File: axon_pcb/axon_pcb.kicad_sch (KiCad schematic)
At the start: 108 parts, among them J1 USB_C_Receptacle, J2 AVR_ISP Header, K1 KEYSW, K10 KEYSW, K11 KEYSW, K12 KEYSW, K13 KEYSW, K14 KEYSW, K15 KEYSW, K16 KEYSW, K17 KEYSW, K18 KEYSW, K19 KEYSW, K2 KEYSW, K20 KEYSW, K21 KEYSW, K22 KEYSW, K23 KEYSW, K24 KEYSW, K25 KEYSW, K26 KEYSW, K27 KEYSW, K28 KEYSW, K29 KEYSW, K3 KEYSW, K30 KEYSW, K31 KEYSW, K32 KEYSW, K33 KEYSW, K34 KEYSW, K35 KEYSW, K36 KEYSW, K37 KEYSW, K38 KEYSW, K39 KEYSW, K4 KEYSW, K40 KEYSW, K41 KEYSW, K42 KEYSW, K43 KEYSW, K44 KEYSW, K45 KEYSW, K46 KEYSW, K5 KEYSW, K6 KEYSW, K7 KEYSW, K8 KEYSW, K9 KEYSW, SW1 RESET, SW2 BOOT, U1 ATmega328P-PU, X1 16MHz

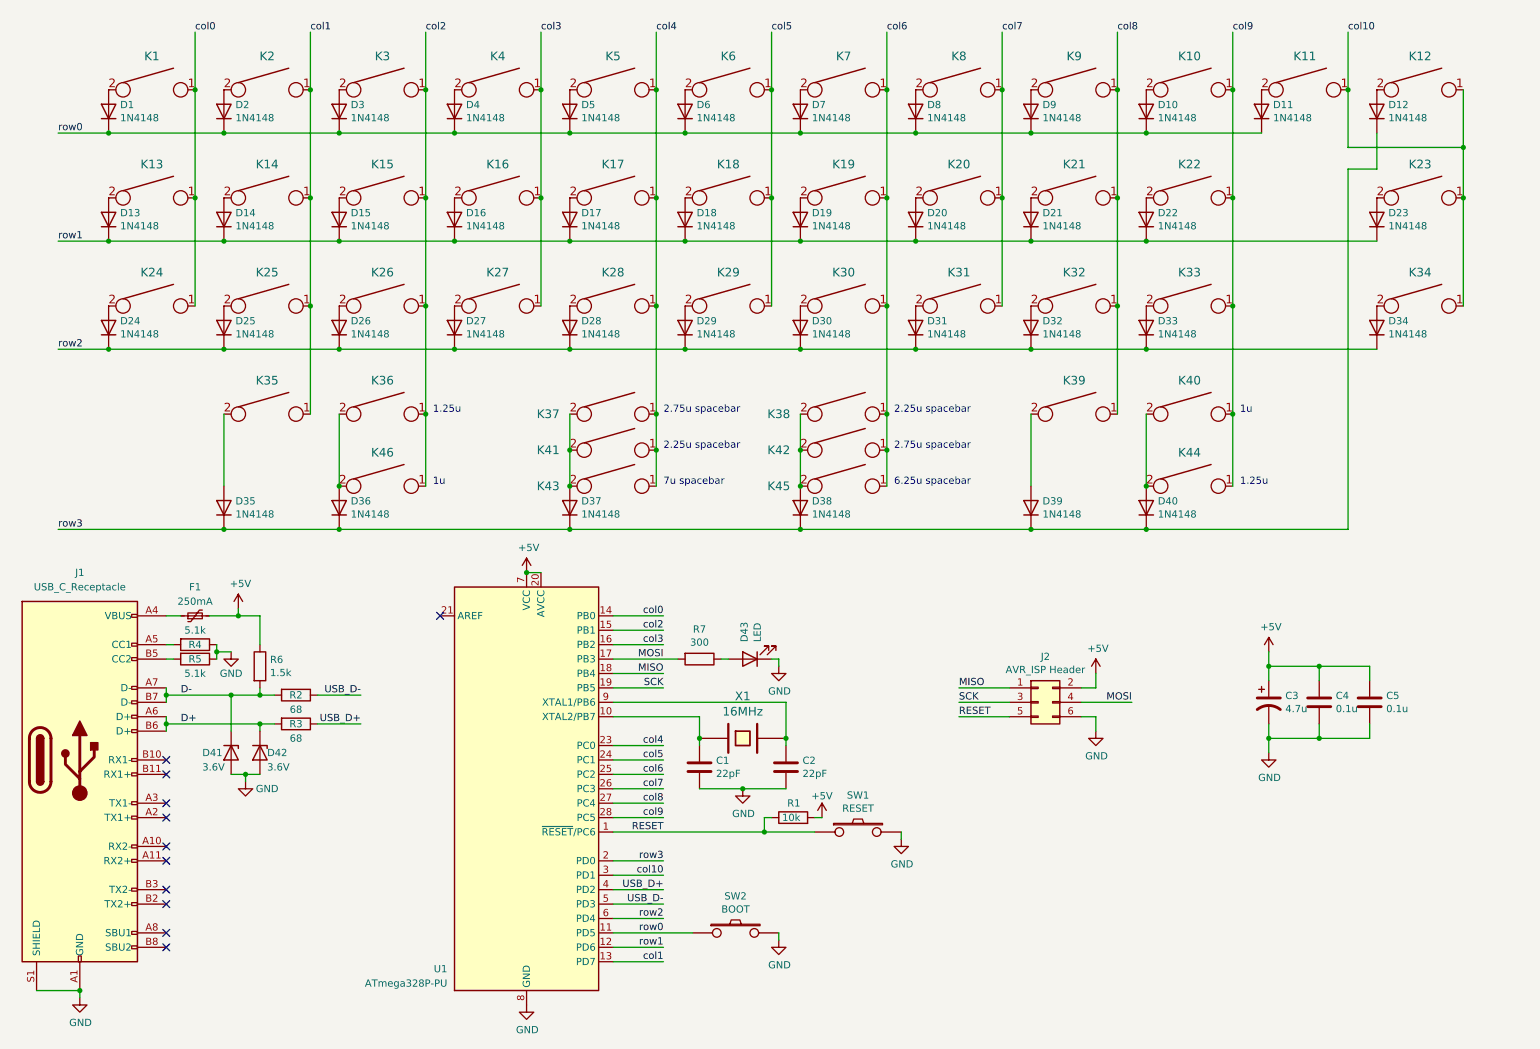
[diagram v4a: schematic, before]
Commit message: enable hardware pwm led dimming
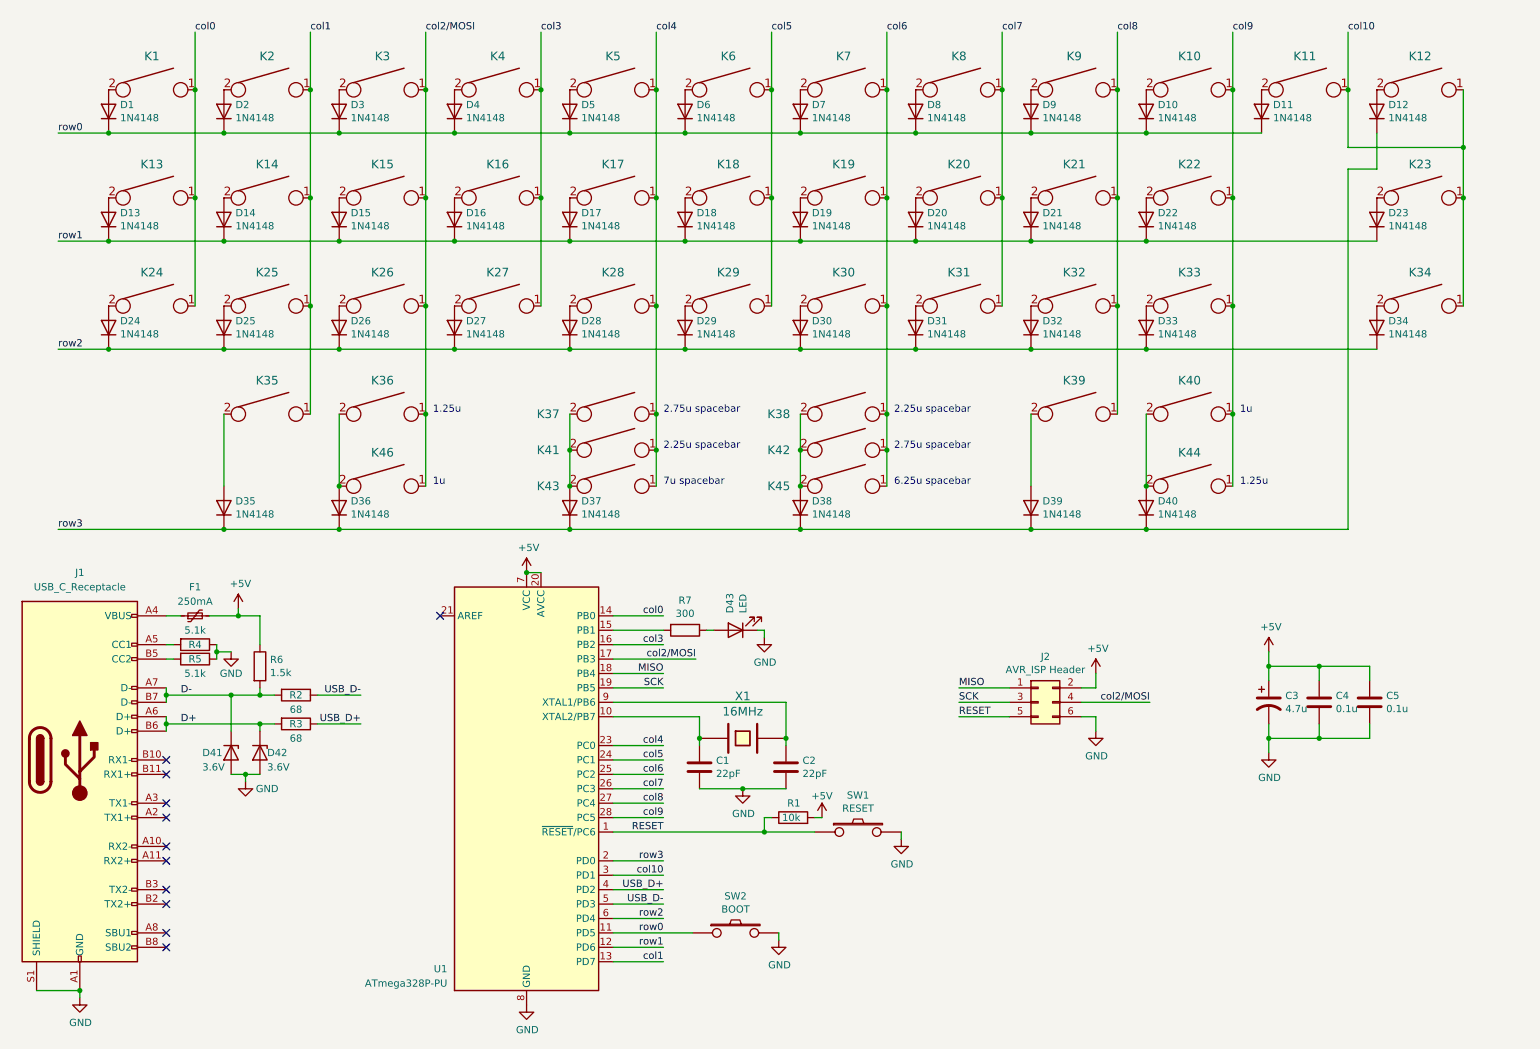
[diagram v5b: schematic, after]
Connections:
- net MOSI renamed col2/MOSI
- net col2/MOSI: now also K15.1, K26.1, K3.1, K36.1, K46.1; no longer R7.2
- removed net col2: K15.1, K26.1, K3.1, K36.1, K46.1, U1.15 (PB1)
- new net: R7.2, U1.15 (PB1)
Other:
- moved on the sheet: D43, R7
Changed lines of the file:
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@@
     (stroke (width 0) (type default) (color 0 0 0 0))
   )
-  (wire (pts (xy 140.97 130.81) (xy 142.24 130.81))
+  (wire (pts (xy 138.43 125.73) (xy 139.7 125.73))
     (stroke (width 0) (type default) (color 0 0 0 0))
   )
@@
     (stroke (width 0) (type default) (color 0 0 0 0))
   )
-  (wire (pts (xy 149.86 130.81) (xy 151.13 130.81))
+  (wire (pts (xy 147.32 125.73) (xy 148.59 125.73))
     (stroke (width 0) (type default) (color 0 0 0 0))
   )
@@
     (stroke (width 0) (type default) (color 0 0 0 0))
   )
-  (wire (pts (xy 121.92 130.81) (xy 133.35 130.81))
+  (wire (pts (xy 121.92 130.81) (xy 136.525 130.81))
     (stroke (width 0) (type default) (color 0 0 0 0))
   )
@@
     (stroke (width 0) (type default) (color 0 0 0 0))
   )
-  (wire (pts (xy 204.47 138.43) (xy 213.36 138.43))
+  (wire (pts (xy 204.47 138.43) (xy 216.535 138.43))
     (stroke (width 0) (type default) (color 0 0 0 0))
   )
@@
     (stroke (width 0) (type default) (color 0 0 0 0))
   )
-  (wire (pts (xy 151.13 130.81) (xy 151.13 132.08))
+  (wire (pts (xy 148.59 125.73) (xy 148.59 127))
     (stroke (width 0) (type default) (color 0 0 0 0))
   )
@@
     (effects (font (size 1.27 1.27)) (justify right bottom))
   )
-  (label "col2" (at 130.81 125.73 180)
-    (effects (font (size 1.27 1.27)) (justify right bottom))
-  )
   (label "col4" (at 129.54 20.32 0)
     (effects (font (size 1.27 1.27)) (justify left bottom))
@@
     (effects (font (size 1.27 1.27)) (justify right bottom))
   )
-  (label "MOSI" (at 130.81 130.81 180)
+  (label "col2{slash}MOSI" (at 136.525 130.81 180)
     (effects (font (size 1.27 1.27)) (justify right bottom))
   )
@@
     (effects (font (size 1.27 1.27)) (justify left bottom))
   )
-  (label "col2" (at 88.9 20.32 0)
+  (label "col2{slash}MOSI" (at 88.9 20.32 0)
     (effects (font (size 1.27 1.27)) (justify left bottom))
   )
@@
     (effects (font (size 1.27 1.27)) (justify left bottom))
   )
-  (label "MOSI" (at 213.36 138.43 180)
+  (label "col2{slash}MOSI" (at 216.535 138.43 180)
     (effects (font (size 1.27 1.27)) (justify right bottom))
   )
@@
     (pin "1")
   )
-  (symbol (lib_id "Device:R") (at 137.16 130.81 270) (unit 1)
-    (in_bom yes) (on_board yes)
-    (property "Reference" "R7" (id 0) (at 137.16 125.5522 90))
-    (property "Value" "300" (id 1) (at 137.16 127.8636 90))
-    (property "Footprint" "Resistor_THT:R_Axial_DIN0204_L3.6mm_D1.6mm_P5.08mm_Horizontal" (id 2) (at 137.16 129.032 90)
-      (effects (font (size 1.27 1.27)) hide)
-    )
-    (property "Datasheet" "~" (id 3) (at 137.16 130.81 0)
-      (effects (font (size 1.27 1.27)) hide)
-    )
-    (pin "1")
-    (pin "2")
-  )
-  (symbol (lib_id "Device:LED") (at 146.05 130.81 180) (unit 1)
-    (in_bom yes) (on_board yes)
-    (property "Reference" "D43" (id 0) (at 145.0594 127.8128 90)
-      (effects (font (size 1.27 1.27)) (justify right))
-    )
-    (property "Value" "LED" (id 1) (at 147.3708 127.8128 90)
-      (effects (font (size 1.27 1.27)) (justify right))
-    )
-    (property "Footprint" "LED_THT:LED_D5.0mm" (id 2) (at 146.05 130.81 0)
-      (effects (font (size 1.27 1.27)) hide)
-    )
-    (property "Datasheet" "~" (id 3) (at 146.05 130.81 0)
-      (effects (font (size 1.27 1.27)) hide)
-    )
-    (pin "1")
-    (pin "2")
-  )
-  (symbol (lib_id "power:GND") (at 151.13 132.08 0) (unit 1)
-    (in_bom yes) (on_board yes)
-    (property "Reference" "#PWR0111" (id 0) (at 151.13 138.43 0)
-      (effects (font (size 1.27 1.27)) hide)
-    )
-    (property "Value" "GND" (id 1) (at 151.257 136.4742 0))
-    (property "Footprint" "" (id 2) (at 151.13 132.08 0)
-      (effects (font (size 1.27 1.27)) hide)
-    )
-    (property "Datasheet" "" (id 3) (at 151.13 132.08 0)
-      (effects (font (size 1.27 1.27)) hide)
-    )
+  (symbol (lib_id "Device:R") (at 134.62 125.73 270) (unit 1)
+    (in_bom yes) (on_board yes)
+    (property "Reference" "R7" (id 0) (at 134.62 120.4722 90))
+    (property "Value" "300" (id 1) (at 134.62 122.7836 90))
+    (property "Footprint" "Resistor_THT:R_Axial_DIN0204_L3.6mm_D1.6mm_P5.08mm_Horizontal" (id 2) (at 134.62 123.952 90)
+      (effects (font (size 1.27 1.27)) hide)
+    )
+    (property "Datasheet" "~" (id 3) (at 134.62 125.73 0)
+      (effects (font (size 1.27 1.27)) hide)
+    )
+    (pin "1")
+    (pin "2")
+  )
+  (symbol (lib_id "Device:LED") (at 143.51 125.73 180) (unit 1)
+    (in_bom yes) (on_board yes)
+    (property "Reference" "D43" (id 0) (at 142.5194 122.7328 90)
+      (effects (font (size 1.27 1.27)) (justify right))
+    )
+    (property "Value" "LED" (id 1) (at 144.8308 122.7328 90)
+      (effects (font (size 1.27 1.27)) (justify right))
+    )
+    (property "Footprint" "LED_THT:LED_D5.0mm" (id 2) (at 143.51 125.73 0)
+      (effects (font (size 1.27 1.27)) hide)
+    )
+    (property "Datasheet" "~" (id 3) (at 143.51 125.73 0)
+      (effects (font (size 1.27 1.27)) hide)
+    )
+    (pin "1")
+    (pin "2")
+  )
+  (symbol (lib_id "power:GND") (at 148.59 127 0) (unit 1)
+    (in_bom yes) (on_board yes)
+    (property "Reference" "#PWR0111" (id 0) (at 148.59 133.35 0)
+      (effects (font (size 1.27 1.27)) hide)
+    )
+    (property "Value" "GND" (id 1) (at 148.717 131.3942 0))
+    (property "Footprint" "" (id 2) (at 148.59 127 0)
+      (effects (font (size 1.27 1.27)) hide)
+    )
+    (property "Datasheet" "" (id 3) (at 148.59 127 0)
+      (effects (font (size 1.27 1.27)) hide)
+    )

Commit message: add encoder support
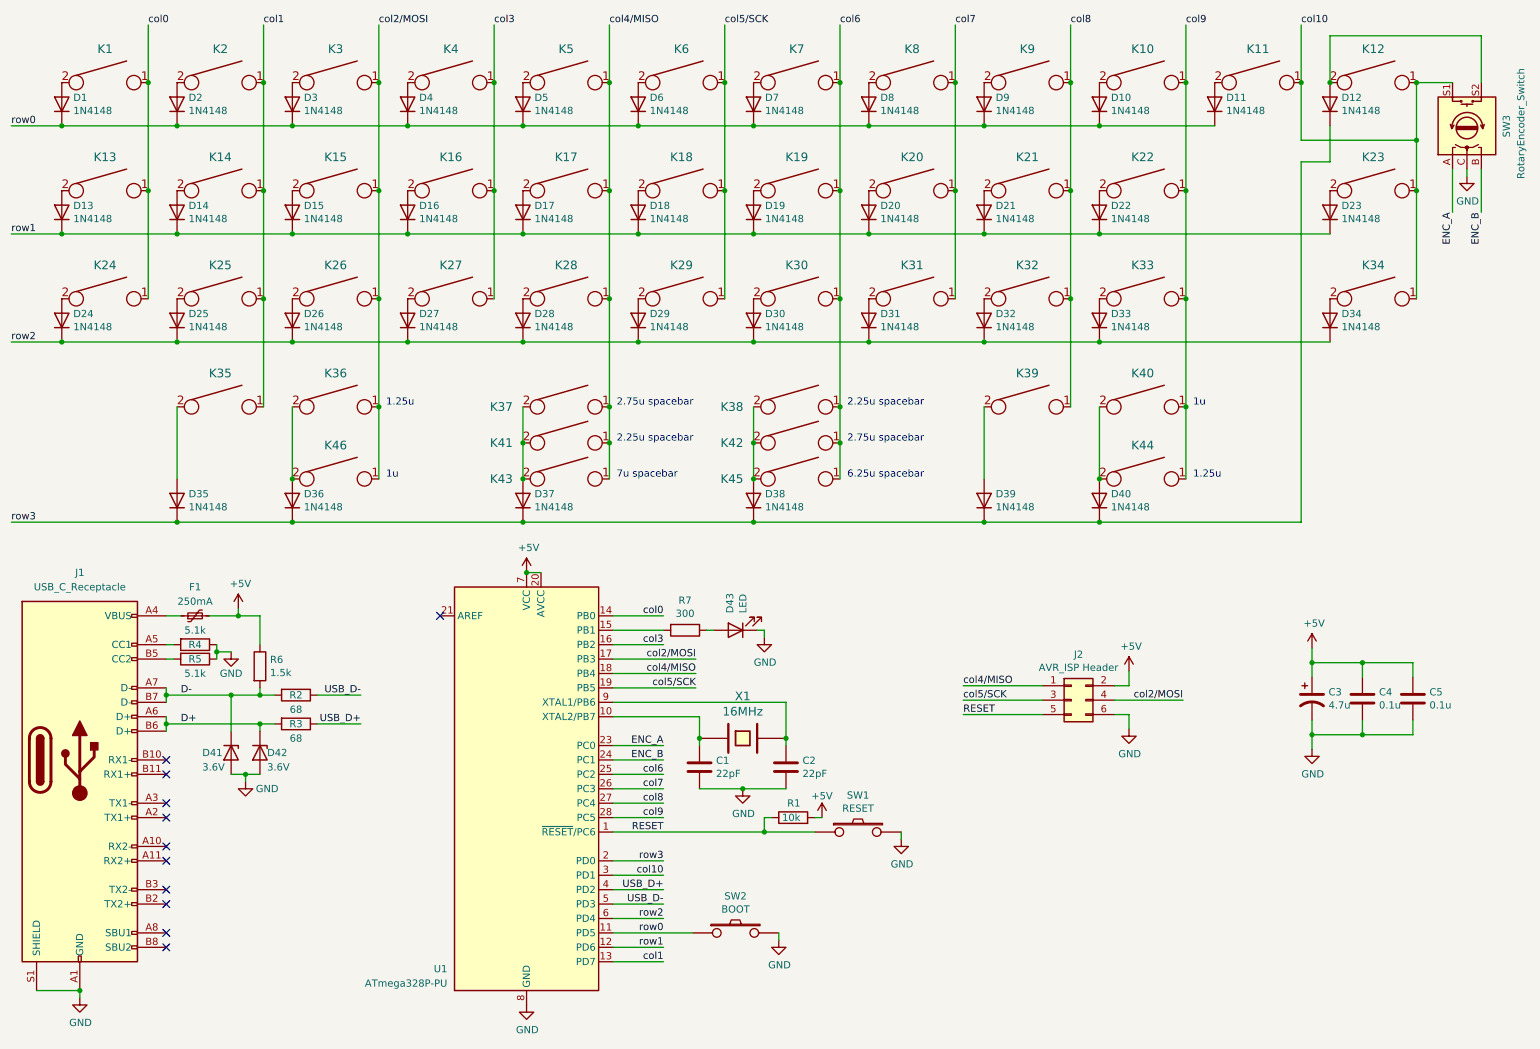
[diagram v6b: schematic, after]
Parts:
- added SW3: RotaryEncoder_Switch, Rotary_Encoder:RotaryEncoder_Alps_EC11E-Switch_Vertical_H20mm, symbol Device:RotaryEncoder_Switch
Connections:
- net GND: now also SW3.C
- net col10: now also SW3.S1
- net at D12.2 (A), K12.2: now also SW3.S2
- net MISO renamed col4/MISO
- net col4/MISO: now also K17.1, K28.1, K37.1, K41.1, K43.1, K5.1
- net SCK renamed col5/SCK
- net col5/SCK: now also K18.1, K29.1, K6.1
- removed net col4: K17.1, K28.1, K37.1, K41.1, K43.1, K5.1, U1.23 (PC0)
- removed net col5: K18.1, K29.1, K6.1, U1.24 (PC1)
- new net ENC_A: SW3.A, U1.23 (PC0)
- new net ENC_B: SW3.B, U1.24 (PC1)
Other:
- moved on the sheet: C3, C4, C5, D1, D10, D11, D12, D13, D14, D15, D16, D17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

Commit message: routing improvement
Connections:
- net ENC_A: now also U1.24 (PC1); no longer U1.23 (PC0)
- net ENC_B: now also U1.3 (PD1); no longer U1.24 (PC1)
- net col10: now also U1.23 (PC0); no longer U1.3 (PD1)
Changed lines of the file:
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@@
     (effects (font (size 1.27 1.27)) (justify right bottom))
   )
-  (label "col10" (at 130.81 168.91 180)
+  (label "col10" (at 130.81 146.05 180)
     (effects (font (size 1.27 1.27)) (justify right bottom))
   )
@@
     (effects (font (size 1.27 1.27)) (justify right bottom))
   )
-  (label "ENC_B" (at 130.81 148.59 180)
+  (label "ENC_B" (at 130.81 168.91 180)
     (effects (font (size 1.27 1.27)) (justify right bottom))
   )
-  (label "ENC_A" (at 130.81 146.05 180)
+  (label "ENC_A" (at 130.81 148.59 180)
     (effects (font (size 1.27 1.27)) (justify right bottom))
   )
